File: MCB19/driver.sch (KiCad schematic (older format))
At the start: 41 parts, among them J611 +BAT_IN, J612 -BAT_IN, J613 +BAT_OUT, J614 -BAT_OUT, Q601 IRFP260N, Q602 IRFP260N, U601 LM5104MNOPB, U602 INA211_DCK_6, U603 LM324

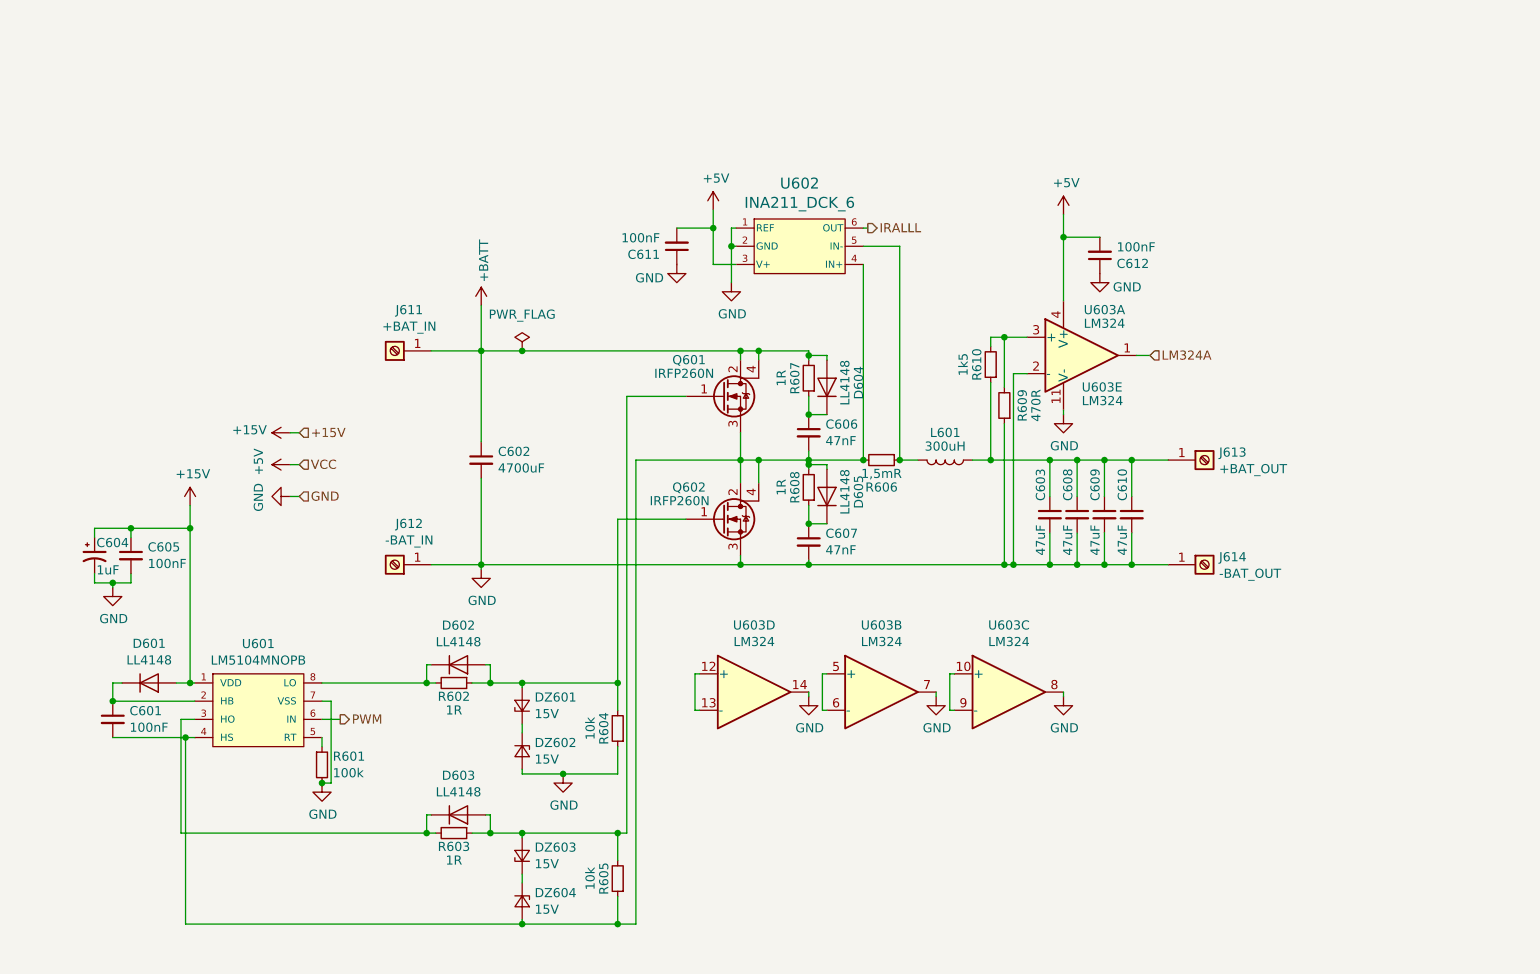
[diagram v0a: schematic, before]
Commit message: Snubber and shunt footprints fixed
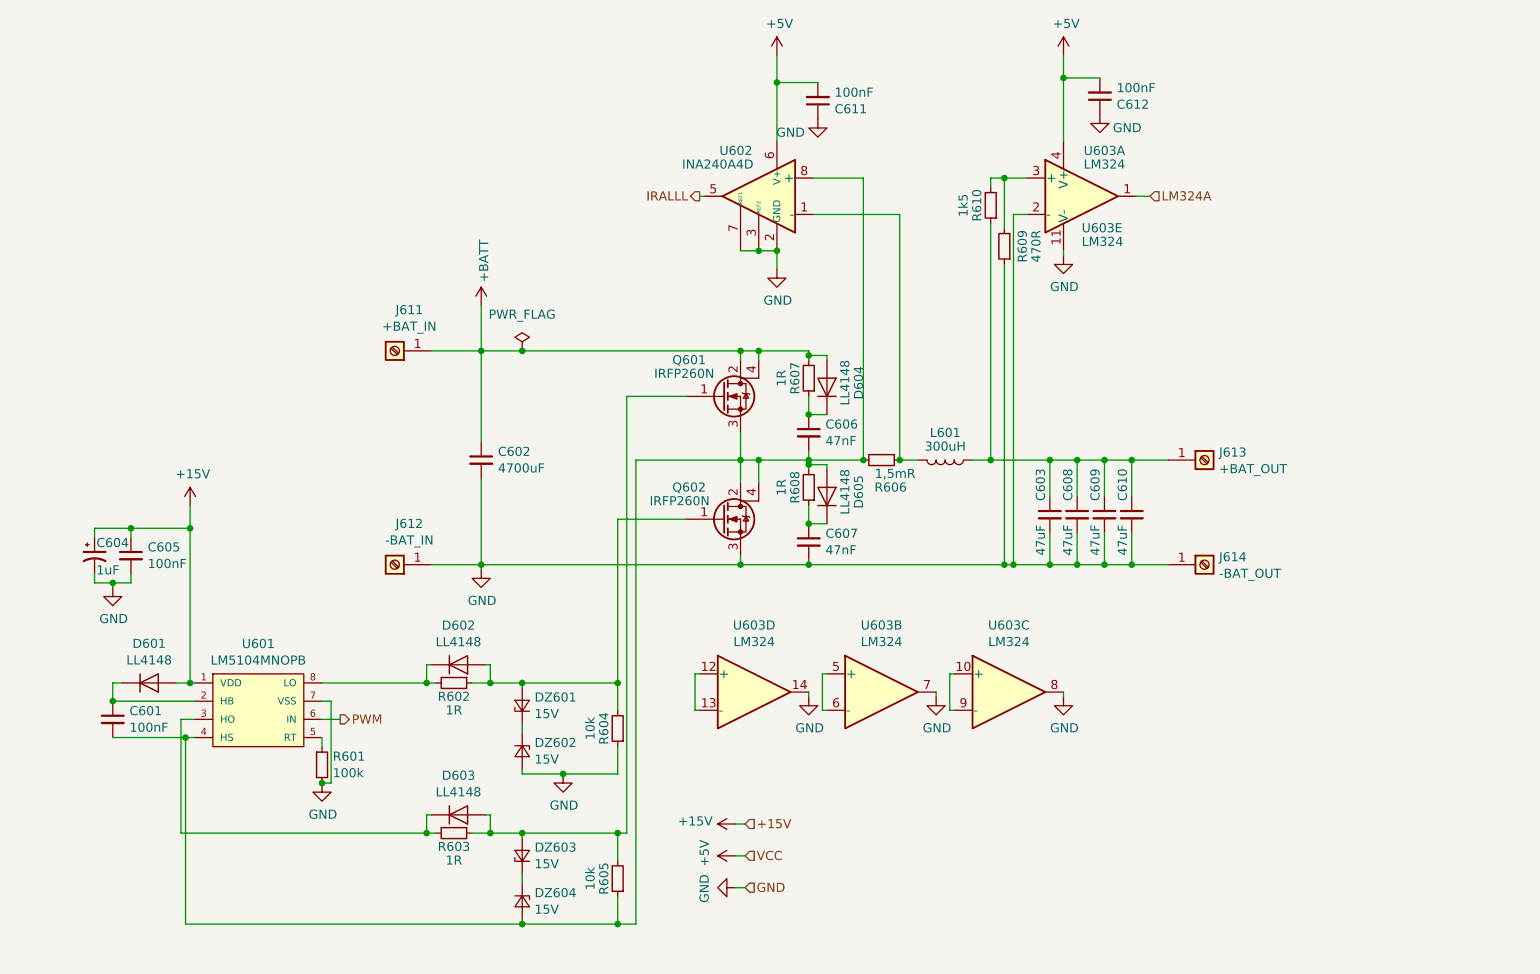
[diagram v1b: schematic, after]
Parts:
- removed U602: INA211_DCK_6, Package_TO_SOT_SMD:SOT-23-6_Handsoldering, symbol MCB19-rescue:INA211_DCK_6-INA211BIDCKR
- added U602: INA240A4D, Package_SO:SOIC-8_3.9x4.9mm_P1.27mm, symbol Amplifier_Current:INA240A4D
- R606: footprint Resistor_SMD:R_2512_6332Metric_Pad1.52x3.35mm_HandSolder -> KicadZeniteSolarLibrary18:R_2512_6432Metric_Reversed
- R607: footprint Resistor_SMD:R_1210_3225Metric_Pad1.42x2.65mm_HandSolder -> Resistor_SMD:R_2512_6332Metric
- R608: footprint Resistor_SMD:R_1210_3225Metric_Pad1.42x2.65mm_HandSolder -> Resistor_SMD:R_2512_6332Metric_Pad1.52x3.35mm_HandSolder
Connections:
- net +5V: now also U602.6 (V+)
- net GND: now also U602.2 (GND), U602.3 (REF2), U602.4 (GND), U602.7 (REF1)
- net IRALLL: now also U602.5
- net at L601.2, R606.1: now also U602.1 (-)
- net at C601.2, C606.2, D605.2 (A)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: now also U602.8 (+)
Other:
- moved on the sheet: C611, C612, R609, R610, U603A, U603E

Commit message: ready for fab
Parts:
- added C613, C614, C617, C618: 4.7u, Capacitor_SMD:C_1206_3216Metric_Pad1.42x1.75mm_HandSolder, symbol Device:C_Small
- added C615, C616, C619, C620: 100n, Capacitor_SMD:C_0805_2012Metric_Pad1.15x1.40mm_HandSolder, symbol Device:C_Small
- added F601: 10A, Fuse:Fuseholder_Cylinder-5x20mm_Stelvio-Kontek_PTF78_Horizontal_Open, symbol Device:Fuse
- added F?: 15A, Fuse:Fuseholder_Cylinder-5x20mm_Stelvio-Kontek_PTF78_Horizontal_Open, symbol Device:Fuse
- C602, C603, C608, C609, C610: symbol Device:C_Small -> Device:CP1_Small
- D604, D605: value LL4148 -> ES2A
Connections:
- net +BATT: now also C613.1, C614.1, C615.1, C616.1, F601.1; no longer J611.1 (Pin_1)
- net GND: now also C613.2, C614.2, C615.2, C616.2, C617.2, C618.2, C619.2, C620.2
- net at C603.1, C608.1, C609.1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: now also C617.1, C618.1, C619.1, C620.1, F?.2; no longer J613.1 (Pin_1)
- new net: F601.2, J611.1 (Pin_1)
- new net: F?.1, J613.1 (Pin_1)
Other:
- moved on the sheet: C601, C604, C605, D601, D602, D603, DZ601, DZ602, DZ603, DZ604, J611, J612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
